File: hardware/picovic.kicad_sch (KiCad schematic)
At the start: 17 parts, among them J1 DB15_Female_HighDensity, J2 Conn_01x06, P1 Mini-DIN_6pins_ver2, U1 74HC14

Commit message: Set variables
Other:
- title: Picovic -> PicoVIC
- moved on the sheet: C1, C2, J1, J2, P1, R1, R10, R2, R3, R4, R5, R6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

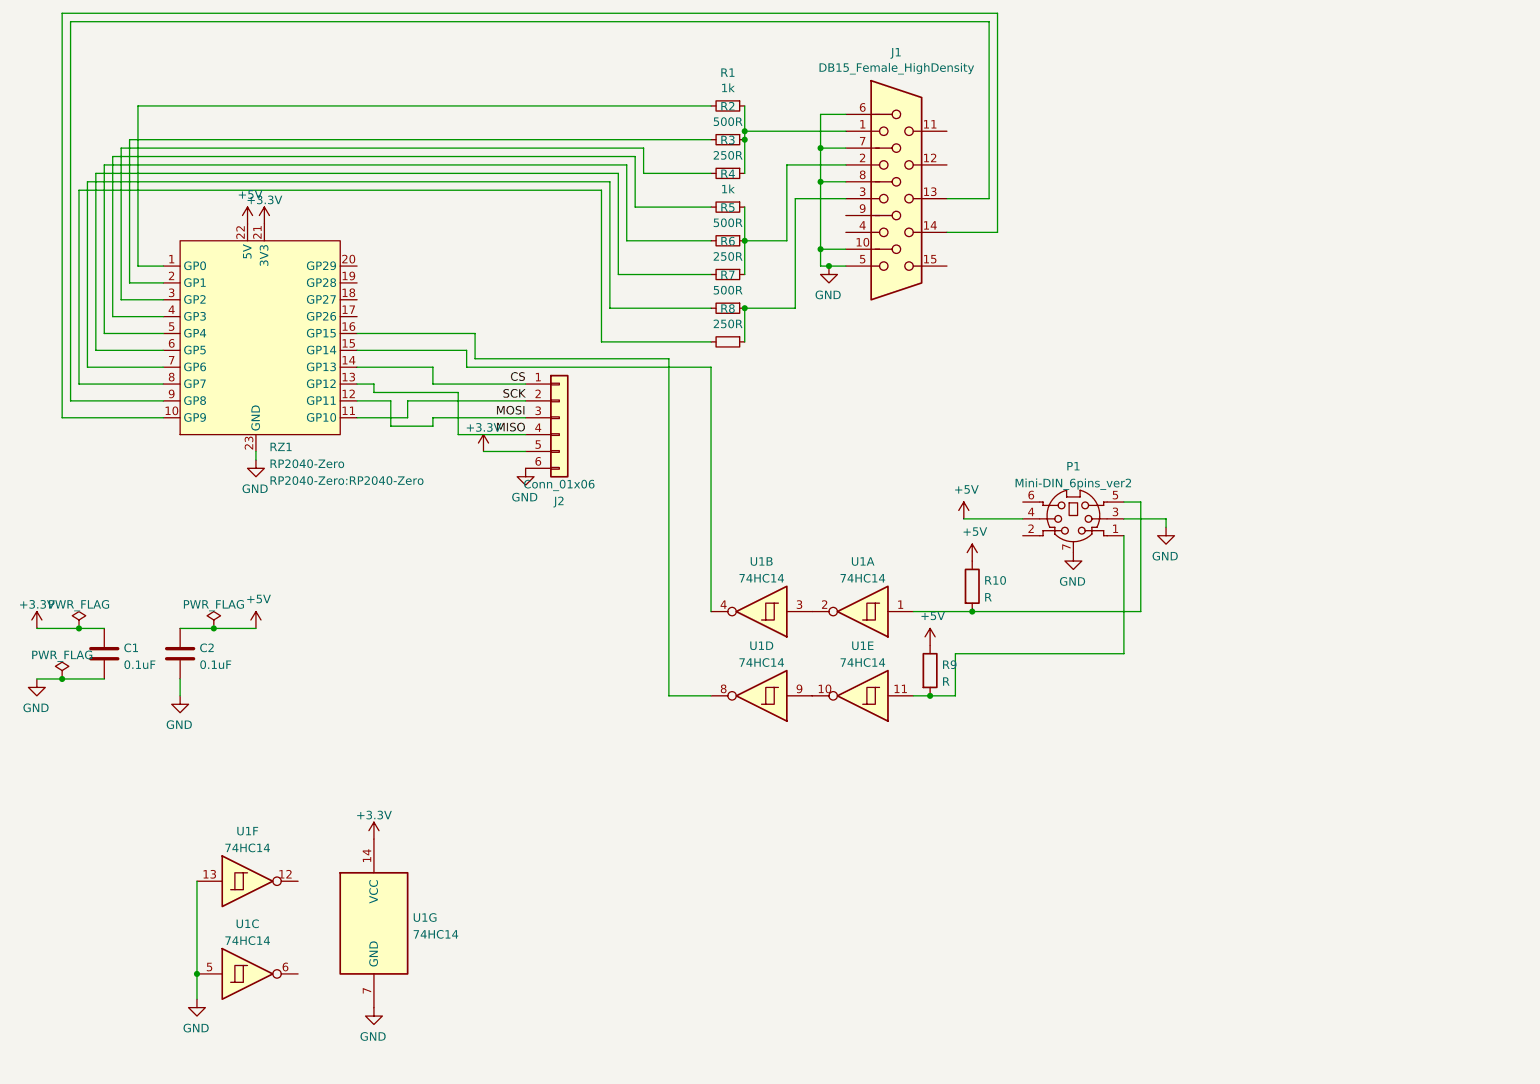
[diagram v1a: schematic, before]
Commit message: Fix i2c pins order
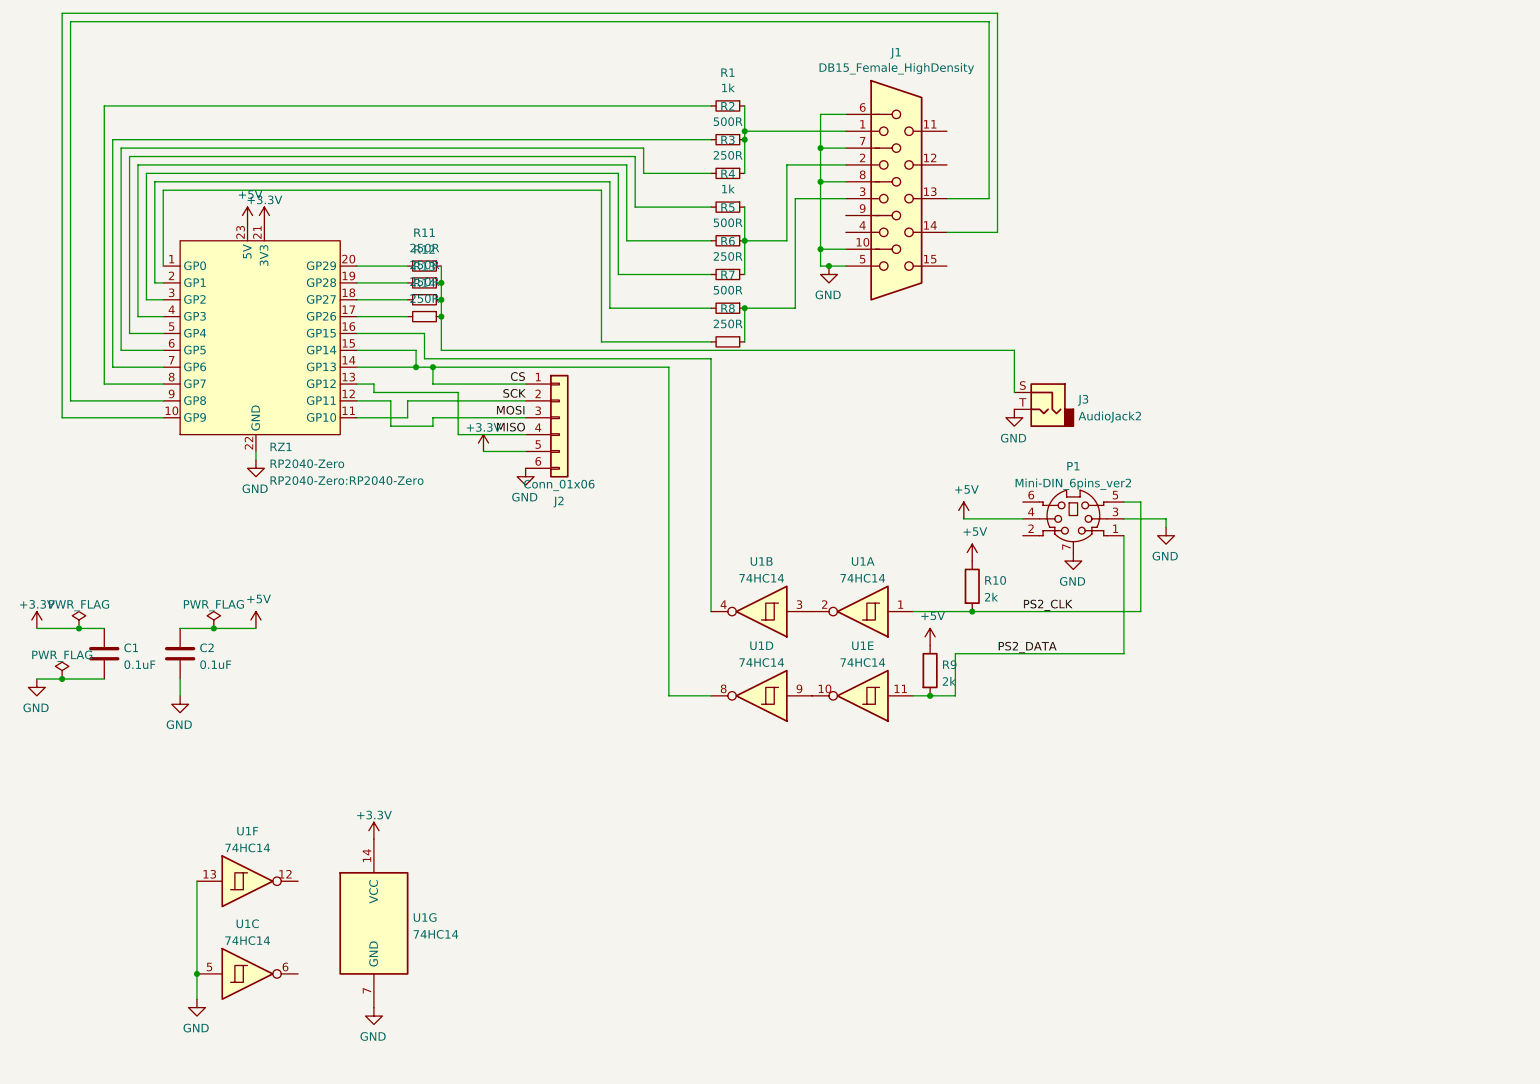
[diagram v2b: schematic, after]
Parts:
- added J3: AudioJack2, symbol Connector:AudioJack2
- added R11, R12, R13, R14: 250R, Resistor_THT:R_Axial_DIN0207_L6.3mm_D2.5mm_P7.62mm_Horizontal, symbol Device:R_Small
- R10, R9: value R -> 2k
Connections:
- net +5V: now also RZ1.23 (5V); no longer RZ1.22 (5V)
- net CS: now also RZ1.15 (GP14), U1.8
- net GND: now also RZ1.22 (GND), J3.T; no longer RZ1.23 (GND)
- net at R2.2: now also RZ1.7 (GP6); no longer RZ1.2 (GP1)
- net at R3.2: now also RZ1.6 (GP5); no longer RZ1.3 (GP2)
- net at R4.2: now also RZ1.5 (GP4); no longer RZ1.4 (GP3)
- net at R5.2: now also RZ1.4 (GP3); no longer RZ1.5 (GP4)
- net at R6.2: now also RZ1.3 (GP2); no longer RZ1.6 (GP5)
- net at R7.2: now also RZ1.2 (GP1); no longer RZ1.7 (GP6)
- net at R1.2: now also RZ1.8 (GP7); no longer RZ1.1 (GP0)
- net at R8.2: now also RZ1.1 (GP0); no longer RZ1.8 (GP7)
- net PS2_DATA: now reaches P1.1, R9.2, U1.11
- net PS2_CLK: now reaches P1.5, R10.2, U1.1
- net at U1.4: now also RZ1.16 (GP15); no longer RZ1.15 (GP14)
- net at RZ1.17 (GP26): now also R14.2
- net at RZ1.18 (GP27): now also R13.2
- net at RZ1.19 (GP28): now also R12.2
- net at RZ1.20 (GP29): now also R11.2
- new net: J3.S, R11.1, R12.1, R13.1, R14.1
